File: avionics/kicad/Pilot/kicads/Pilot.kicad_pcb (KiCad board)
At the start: 6 copper layers, 55 x 35 mm, 120 parts, among them X2Y-CAN 4.7nF X2Y, X2Y-RS485 4.7nF X2Y

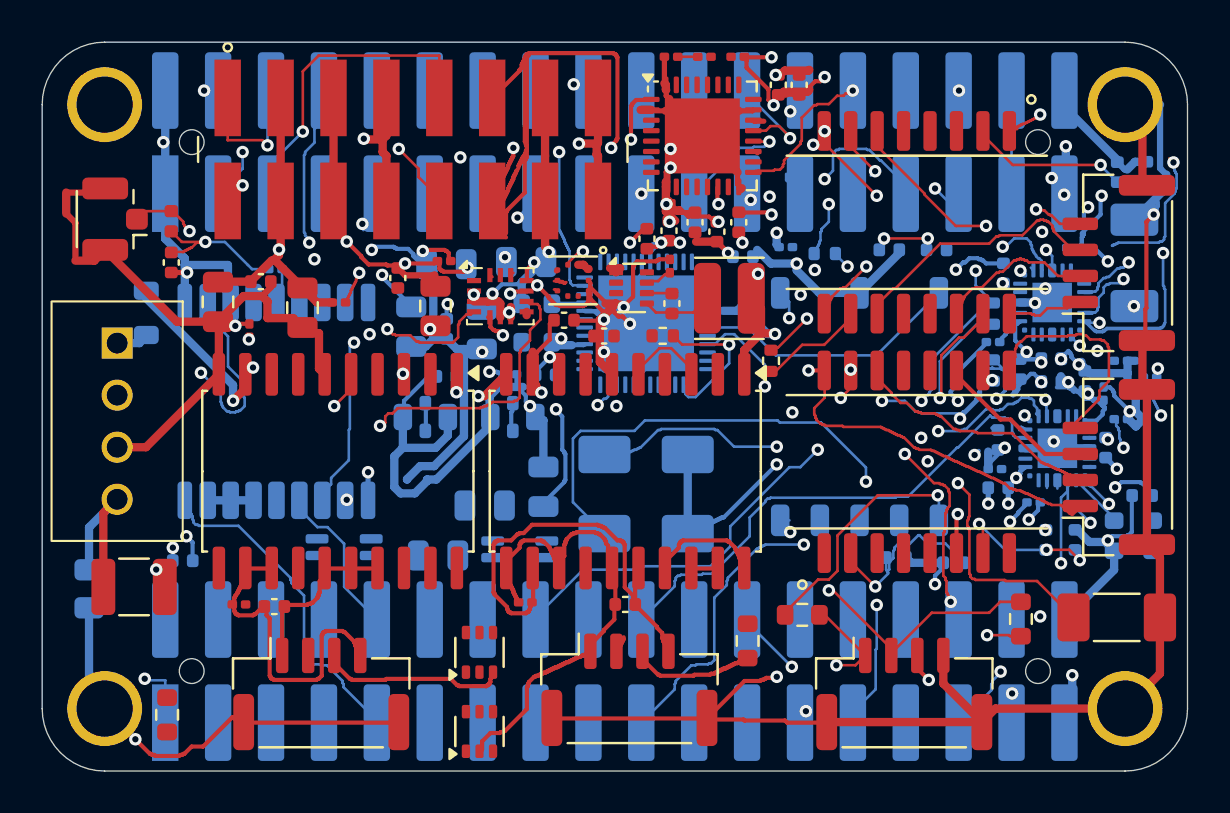
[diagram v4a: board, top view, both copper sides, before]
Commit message: feat(pilot): PB2-I re-map, TPSM828224 3V3, keep-copper re-floorplan, AM625/MSPM0 header capability docs
Pilot (branch pilot-refloorplan, owner S. Griffing decisions 2026-10-17; implemented by
Claude Opus 5.5):
- 3V3 rail -> TI TPSM828224SILR MicroSiP module [REF-PWR-008]; C-3V3 caps chosen on DC-bias
  curves (Taiyo Yuden MSASJ168BC6226MTNA01 [REF-PWR-011]); SIL0010D land + STEP.
- Keep-copper re-floorplan for ISOW1044/ISOW1412 sec 13.1 bubbles (iso_zones_pilot.py,
  refloorplan_pilot.py, refloorplan_keep_copper.sh); PCB DRC 0 / parity 0 / 107 unconnected
  at that point (PCB predates the header re-map below; re-sync pending in avionics/WBS.md).
- PB2-I header re-map from BeagleBoard sources [REF-SENSOR-021, REF-SENSOR-041 sec 4.2,
  REF-SENSOR-047]; TSM-DV-LC rail footprints mirrored so pin 1 lands on the official row
  on B.Cu; GNSS replaced by JST-GH expansion ports; Ethernet ring = DP83825I on RMII2 +
  USB NIC on USB1 (CH397A placeholder; AX88772E pending, WCH fails the AGENTS.md sec 5
  sourcing rule).

AM625 / MSPM0L1105 capability check (owner request 2026-10-17):
- New avionics/kicad/PB2I_AM625_HEADER_CAPABILITIES.md + extracted JSON from TI SPRSP58C
  Table 5-1 / sec 5.3.1 [REF-SENSOR-049], SPRUIV7C sec 1.4.12 [REF-SENSOR-050], MSPM0L1105
  SLASEX5C [REF-SENSOR-051] and SLAU847F sec 2.4.1.2 [REF-SENSOR-052]: CPSW3G has two
  external ports but only port 2 reaches the header; 3 CAN-FD reachable; 17 dual-ball
  header pins; 8 AIN pins also tied to the MSPM0 (SWCLK pull-down on P2-35 after POR).
- PB2_HEADER_PINMAP.md sec 1 second balls on P1-2/4/6 added and footnote corrected.
- Reviewed by ce-doc-review (coherence + feasibility subagents, Claude Haiku / Opus 5.5);
  findings applied. ce-compound-refresh: new learning
  docs/solutions/conventions/pb2-header-capability-from-soc-datasheet-not-srm-summary.md,
  two stale "Pilot still has 2.54 mm rails" notes updated, CONCEPTS.md "Shared Header Pin".

Not committed: avionics/datasheets/spruiv7c.pdf (129 MB, abov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
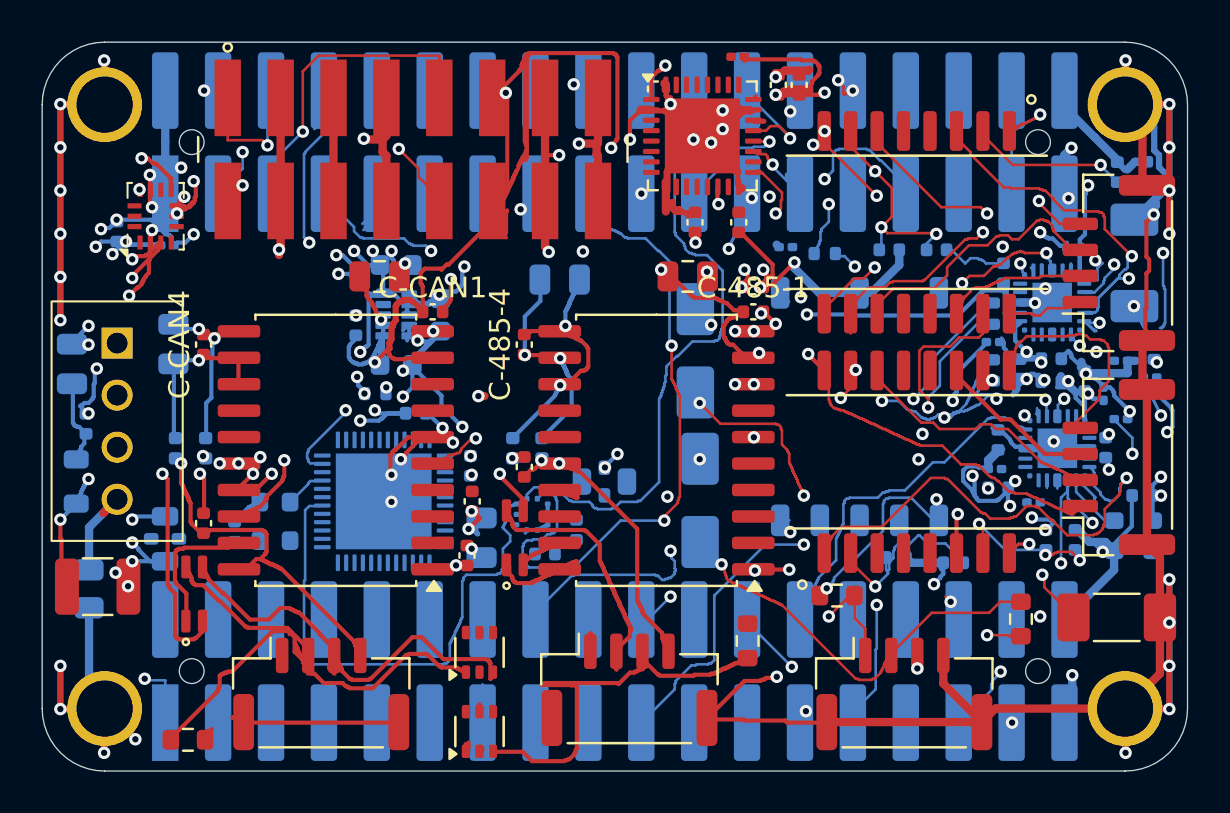
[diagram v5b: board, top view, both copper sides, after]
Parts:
- removed the C-3V3-IN at (144.2, 98.1)
- removed C-ANT: 10nF X7R, Capacitor_SMD:C_0402_1005Metric
- removed C-BST, C-GPS2: 100nF, Capacitor_SMD:C_0402_1005Metric
- removed C-GPS1: 10uF 6.3V X5R, Capacitor_SMD:C_0805_2012Metric
- removed C-SS: 10nF, Capacitor_SMD:C_0201_0603Metric
- removed GPS: MAX-M10S-00B, RF_GPS:ublox_MAX
- removed J-ANT: U.FL-R-SMT-1, Connector_Coaxial:U.FL_Hirose_U.FL-R-SMT-1_Vertical
- removed L-3V3: 3.3uH 2.25A, Serenity-Custom:L_WE-MAPI_3015
- removed L-ANT: 27nH, Inductor_SMD:L_0402_1005Metric
- removed R-ANT: 10R, Resistor_SMD:R_0201_0603Metric
- removed R-EN3: 100k, Resistor_SMD:R_0201_0603Metric
- removed R-FB3H: 100k 1%, Resistor_SMD:R_0201_0603Metric
- removed R-FB3L: 32.4k 1%, Resistor_SMD:R_0201_0603Metric
- added C-3V3-IN: 22uF 6.3V X6S, Capacitor_SMD:C_0603_1608Metric, B.Cu at (138.0, 103.0)
- added FB-485-G: 330R@100MHz, Inductor_SMD:L_0402_1005Metric, B.Cu at (143.6, 107.0)
- added FB-485-V: 330R@100MHz, Inductor_SMD:L_0402_1005Metric, B.Cu at (145.0, 107.0)
- added FB-CAN-G: 330R@100MHz, Inductor_SMD:L_0402_1005Metric, B.Cu at (128.8, 107.0)
- added FB-CAN-V: 330R@100MHz, Inductor_SMD:L_0402_1005Metric, B.Cu at (127.4, 107.0)
- BARO, C-1553B, C-3V3-HF, C-50M, C-BARO1, C-IMU1, C-IMU2, C-IN2, C-IN3, R-1553IRQ, R-BS1R: moved to B.Cu
- C-3V3-O1: value 22uF 6.3V X5R -> 22uF 6.3V X6S; footprint Capacitor_SMD:C_0805_2012Metric -> Capacitor_SMD:C_0603_1608Metric
- C-3V3-O2: value 22uF 6.3V X5R -> 22uF 6.3V X6S; footprint Capacitor_SMD:C_0805_2012Metric -> Capacitor_SMD:C_0603_1608Metric; moved to B.Cu
- C-485-1: footprint Capacitor_SMD:C_0201_0603Metric -> Capacitor_SMD:C_0402_1005Metric; moved to F.Cu
- C-485-2, C-485-3, C-CAN3, CMC-CAN, CMC-RS485: moved to F.Cu
- C-485-4, C-CAN1, C-CAN4: footprint Capacitor_SMD:C_0201_0603Metric -> Capacitor_SMD:C_0402_1005Metric
- U-3V3: value TPS62933DRLR -> TPSM828224SILR; footprint Package_TO_SOT_SMD:SOT-583-8 -> Serenity-Custom:TI_SIL0010D_uSiP-10_2.0x2.5mm_P0.5mm; moved to B.Cu
- moved C-50M 20.1 mm to (130.2, 111.0), turned to 90 degrees
- moved R-BS1R 18.4 mm to (174.4, 102.2)
- moved IMU 17.0 mm to (126.4, 95.9), turned to 90 degrees
- moved C-1553B 16.9 mm to (138.9, 105.3), turned to 0 degrees
- moved C-1553A 16.5 mm to (141.6, 107.8), turned to 90 degrees
- moved C-CAN5 16.3 mm to (127.3, 102.0), turned to 90 degrees
- moved C-1553D 16.1 mm to (141.7, 109.5)
- moved C-BARO1 15.9 mm to (145.1, 112.1), turned to 0 degrees
- moved X-50M 15.8 mm to (132.2, 110.5)
- moved 1553-XCVR 15.2 mm to (137.4, 109.5)
- moved R-1553IRQ 14.1 mm to (137.0, 104.4)
- moved X2Y-CAN 13.8 mm to (126.9, 111.3), turned to 90 degrees
- moved C-IMU1 13.7 mm to (124.6, 96.6)
- moved C-IMU2 13.3 mm to (127.0, 97.2), turned to 0 degrees
- moved C-1553C 13.2 mm to (142.1, 111.3), turned to -90 degrees
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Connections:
- C-485-4 pad 1: VCC2_RS485 -> VCC2_RS485_DCDC
- C-485-4 pad 2: GND2_RS485 -> GND2_RS485_DCDC
- C-485-5 pad 1: VCC2_RS485 -> VCC2_RS485_DCDC
- C-485-5 pad 2: GND2_RS485 -> GND2_RS485_DCDC
- C-CAN4 pad 1: VCC2_CAN -> VCC2_CAN_DCDC
- C-CAN4 pad 2: GND2_CAN -> GND2_CAN_DCDC
- C-CAN5 pad 1: VCC2_CAN -> VCC2_CAN_DCDC
- C-CAN5 pad 2: GND2_CAN -> GND2_CAN_DCDC
- CAN-TR pad 11: GND2_CAN -> GND2_CAN_DCDC
- CAN-TR pad 12: VCC2_CAN -> VCC2_CAN_DCDC
- CAN-TR pad 13: VCC2_CAN -> VCC2_CAN_DCDC
- PB2-P1 pad 31: UART_GPS_RX -> (no net)
- PB2-P1 pad 32: UART_GPS_TX -> (no net)
- PB2-P2 pad 10: GPS_TIMEPULSE -> (no net)
- PB2-P2 pad 9: GPS_RESETN -> (no net)
- RS485 pad 11: GND2_RS485 -> GND2_RS485_DCDC
- RS485 pad 12: VCC2_RS485 -> VCC2_RS485_DCDC
- RS485 pad 13: GND2_RS485 -> GND2_RS485_DCDC
- U-3V3 pad 1: GND -> +5V
- U-3V3 pad 2: U3V3_EN -> +5V
- U-3V3 pad 4: GND -> (no net)
- U-3V3 pad 5: SW_3V3 -> +3V3
- U-3V3 pad 6: BST_3V3 -> +3V3
- U-3V3 pad 7: SS_3V3 -> +3V3
- U-3V3 pad 8: FB_3V3 -> +3V3
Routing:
- net PGND: track 189.0 -> 423.9 mm, vias 6 -> 27
- net UART_GPS_TX: track 45.9 -> 0.00 mm, vias 2 -> 0
- net +3V3: track 87.3 -> 132.9 mm, vias 37 -> 45
- net UART_GPS_RX: track 42.7 -> 0.00 mm, vias 2 -> 0
- net IMU_INT2: track 37.5 -> 1.19 mm, vias 3 -> 1
- net BARO_INT: track 0.00 -> 32.1 mm, vias 0 -> 2
- net SPI0_CS_BARO: track 0.12 -> 30.3 mm
- net CAN_H_F: track 0.00 -> 30.1 mm
- net GND: track 241.3 -> 211.2 mm, vias 48 -> 72
- net SPI0_MISO: track 13.3 -> 42.6 mm, vias 2 -> 3
- net GND2_RS485: track 25.6 -> 1.89 mm, vias 0 -> 3
- net ETH2_TXP: track 0.10 -> 23.5 mm, vias 0 -> 1
- net RMII1_RX_ER: track 24.0 -> 2.31 mm, vias 0 -> 1
- net CAN_L: track 0.00 -> 21.2 mm, vias 0 -> 2
- net ETH_LINE_CRX: track 5.11 -> 25.4 mm, vias 0 -> 2
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
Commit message: refactor(avionics): align Pilot + TACCO header pins and Ethernet names to BeagleBoard / TI naming
Owner decisions 2026-10-17 (S. Griffing; implemented by Claude Opus 5.5):
- REJECTED: second/third CAN-FD bus (the fleet's four buses already cover the need) and
  moving RMII2/DSHOT off the MSPM0-shared AIN pins (RMII2 has no other balls, SPRSP58C
  Table 5-5 [REF-SENSOR-049]; free PRU pins sit under the P2 isolation band).
- PB2 header symbol pins P1..P36 -> BeagleBoard SRM designators P1.01..P2.36
  [REF-SENSOR-041 sec 4.2] on both boards.
- Ethernet ring parts/nets -> TI interface names [REF-SENSOR-049 sec 5.3.1]: PHY-RMII2,
  T-RMII2, ETH_RMII2_*, RMII2_PHY_RSTN/INTRN, C-/R-RMII2-* (both boards); NIC-USB1, T-USB1,
  ETH_USB1_*, C-USB1-*, J-ETH-RMII2 / J-ETH-USB1 (Pilot).
- New avionics/kicad/align_pb2_ti_names.py does the exact-token rename across generators,
  schematics, symbol libraries, PCBs, netlists, project netclasses and scripts. Pilot's
  schematic was regenerated from the edited generator and matched the text rename
  (modulo UUIDs). ERC / DRC / schematic-parity counts unchanged and the Pilot parity item
  set is identical after renaming (Pilot 0 / 43 / 112 pre-existing, PCB re-sync pending;
  TACCO 0 / 5 / 0).
- Refdes-prefix parent tables made specific so the Bob-Smith parts stay with their
  transformer/connector. Unused imports removed in gen_pilot_pcb.py / gen_tacco_pcb.py.

Co-Authored-By: Claude Opus 5.5 <noreply@anthropic.com>
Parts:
- renumbered C-P1-A1 to C-RMII2-A1, C-P1-A2 to C-RMII2-A2, C-P1-A3 to C-RMII2-A3, C-BS1 to C-RMII2-BS, C-P1-CRD1 to C-RMII2-CRD1, C-P1-CRD2 to C-RMII2-CRD2, C-P1-CTD1 to C-RMII2-CTD1, C-P1-CTD2 to C-RMII2-CTD2, C-P1-IO1 to C-RMII2-IO1, C-P1-IO2 to C-RMII2-IO2, C-P1-IO3 to C-RMII2-IO3, C-BS2 to C-USB1-BS, ETH1 to J-ETH-RMII2, ETH2 to J-ETH-USB1, ETH1-PHY to PHY-RMII2, R-P1-AD0 to R-RMII2-AD0, R-BS1R to R-RMII2-BSR, R-BS1T to R-RMII2-BST, R-P1-RBIAS to R-RMII2-RBIAS, R-BS2R to R-USB1-BSR, R-BS2T to R-USB1-BST, T-ETH to T-RMII2, T-ETH2 to T-USB1
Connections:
- net ETH1-PHY_RBIAS renamed PHY-RMII2_RBIAS
- net ETH2_BS renamed ETH_USB1_BS
- net ETH2_CRD renamed ETH_USB1_CRD
- net ETH2_CTD renamed ETH_USB1_CTD
- net ETH2_LINE_CRX renamed ETH_USB1_LINE_CRX
- net ETH2_LINE_CTX renamed ETH_USB1_LINE_CTX
- net ETH2_LINE_RXN renamed ETH_USB1_LINE_RXN
- net ETH2_LINE_RXP renamed ETH_USB1_LINE_RXP
- net ETH2_LINE_TXN renamed ETH_USB1_LINE_TXN
- net ETH2_LINE_TXP renamed ETH_USB1_LINE_TXP
- net ETH2_RXN renamed ETH_USB1_RXN
- net ETH2_RXP renamed ETH_USB1_RXP
- net ETH2_TXN renamed ETH_USB1_TXN
- net ETH2_TXP renamed ETH_USB1_TXP
- net ETH_BS renamed ETH_RMII2_BS
- net ETH_CRD renamed ETH_RMII2_CRD
- net ETH_CTD renamed ETH_RMII2_CTD
- net ETH_LINE_CRX renamed ETH_RMII2_LINE_CRX
- net ETH_LINE_CTX renamed ETH_RMII2_LINE_CTX
- net ETH_LINE_RXN renamed ETH_RMII2_LINE_RXN
- net ETH_LINE_RXP renamed ETH_RMII2_LINE_RXP
- net ETH_LINE_TXN renamed ETH_RMII2_LINE_TXN
- net ETH_LINE_TXP renamed ETH_RMII2_LINE_TXP
- net ETH_RXN renamed ETH_RMII2_RXN
- net ETH_RXP renamed ETH_RMII2_RXP
- net ETH_TXN renamed ETH_RMII2_TXN
- net ETH_TXP renamed ETH_RMII2_TXP
- net PHY1_INTRN renamed RMII2_PHY_INTRN
- net PHY1_RSTN renamed RMII2_PHY_RSTN

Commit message: wip(pilot): save in-progress KiCad edits before merge with pilot-gh-tvs
Co-Authored-By: Claude Sonnet 5.5 <noreply@anthropic.com>
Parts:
- moved C-1553D 0.20 mm to (141.5, 109.7)
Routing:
- net RS485_DE: track 0.34 -> 33.7 mm, vias 0 -> 2
- net SPI0_CLK: track 4.03 -> 35.7 mm
- net RS485_RX: track 0.00 -> 28.5 mm, vias 0 -> 2
- net CAN_STB: track 0.15 -> 23.5 mm, vias 0 -> 2
- net GND: track 211.2 -> 230.0 mm, vias 72 -> 71
- net +3V3: track 132.9 -> 147.6 mm
- net SPI0_MISO: track 42.6 -> 28.4 mm, vias 3 -> 5
- net ETH_USB1_RXN: track 1.34 -> 9.00 mm, vias 1 -> 2
- net PGND: track 423.9 -> 416.5 mm
- net BARO_INT: track 32.1 -> 26.2 mm
- net +5V: track 150.6 -> 145.2 mm
- net BUS_1553_P: track 21.0 -> 24.0 mm
- net MCAN0_RX: track 18.7 -> 16.2 mm
- net VCC2_RS485_DCDC: track 10.3 -> 11.2 mm
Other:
- copper layers 6 -> 8
